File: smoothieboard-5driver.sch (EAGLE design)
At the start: 304 parts, among them IC1 LPC1769, IC10 LM1117-3.3V, IC11 78L12F, IC12 A4982, IC13 R-78E-5.0, IC14 TC4427, IC15 TC4427, IC2 A4982, IC3 A4982, IC4 MCP44X1, IC5 A4982, IC6 A4982, IC9 MCP44X1, J10 POWER_JACKSMD, Q1 BSL207SP, Q10 SUD50P04-08-GE3, Q2 12MHz, Q3 25MHz, Q4 ZXMN4A06, Q5 AOT240L, Q6 AOT240L, Q7 AOT240L, Q8 ZXMN4A06, Q9 ZXMN4A06, U1 USD-SOCKETNEW, X14 USBPTH

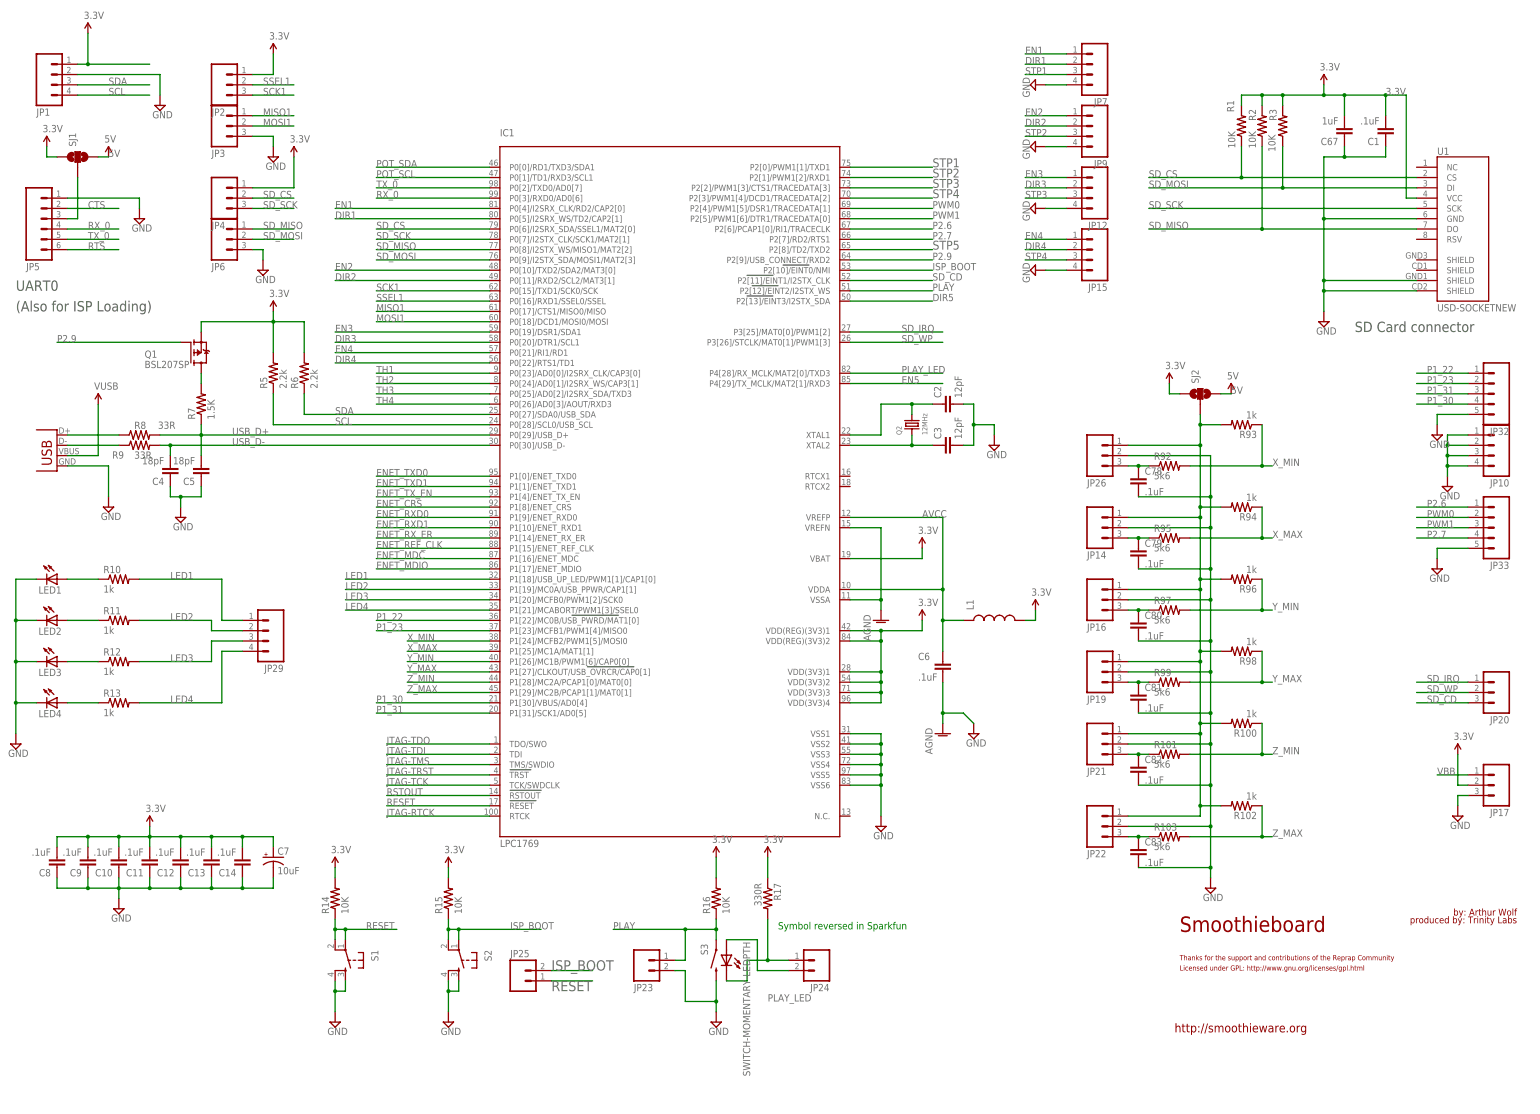
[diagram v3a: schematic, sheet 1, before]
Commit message: Updated R-78 footprint, i2c V select, orientation marker to ic15, silk updates
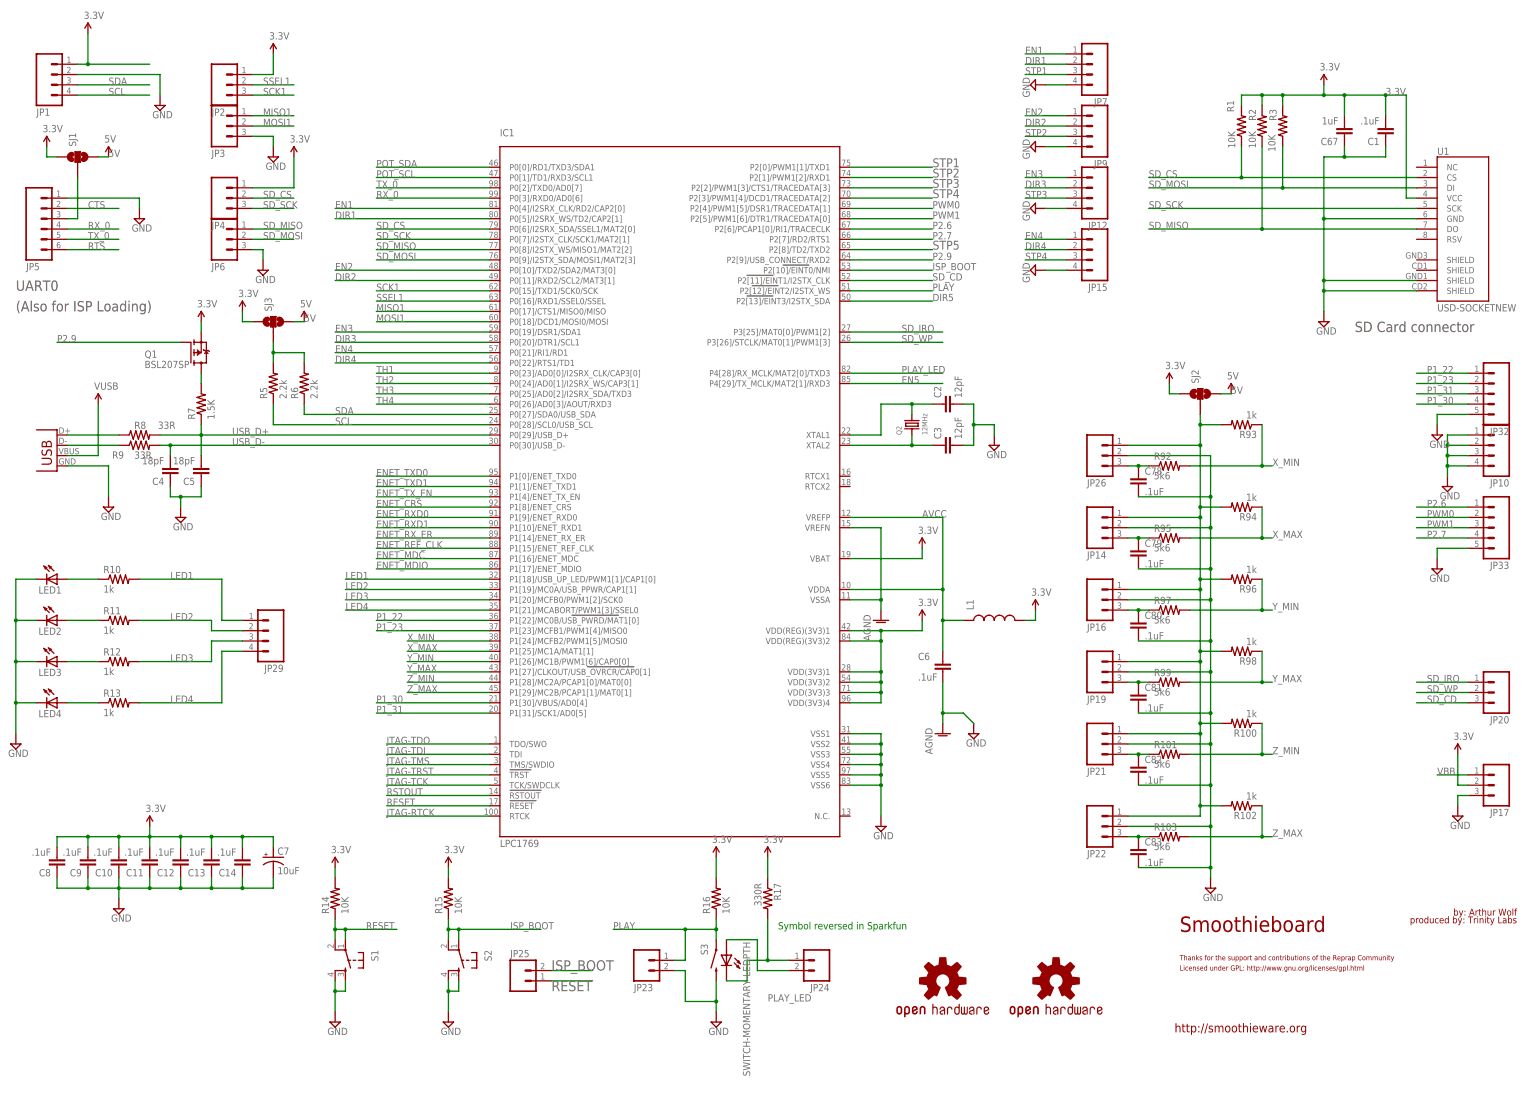
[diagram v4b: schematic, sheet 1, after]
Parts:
- added SJ3: (no value), SparkFun:SOLDERJUMPER_2WAYS
- added U$8, U$9: OSHW-LOGOL, SparkFun-Aesthetics:OSHW-LOGOL
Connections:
- new net N$124: R5.2, R6.2, SJ3.2
- net 3.3V: now also SJ3.1; no longer R5.2, R6.2
- net 5V: now also SJ3.3
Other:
- moved on the sheet: R5, R6
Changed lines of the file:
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@@
 <?xml version="1.0" encoding="utf-8"?>
 <!DOCTYPE eagle SYSTEM "eagle.dtd">
-<eagle version="6.2">
+<eagle version="6.3">
 <drawing>
 <settings>
@@
 <part name="R102" library="resistor" deviceset="R-US_" device="R0603" value="1k"/>
 <part name="R103" library="resistor" deviceset="R-US_" device="R0603" value="5k6"/>
+<part name="SJ3" library="SparkFun" deviceset="SOLDERJUMPER_2WAY" device="S"/>
+<part name="P+40" library="SparkFun" deviceset="3.3V" device=""/>
+<part name="U$2" library="SparkFun" deviceset="5V" device=""/>
+<part name="U$8" library="SparkFun-Aesthetics" deviceset="OSHW-LOGO" device="L"/>
+<part name="U$9" library="SparkFun-Aesthetics" deviceset="OSHW-LOGO" device="L"/>
 </parts>
 <sheets>
@@
 <instance part="SUPPLY58" gate="GND" x="119.38" y="7.62"/>
 <instance part="SUPPLY61" gate="GND" x="43.18" y="205.74"/>
-<instance part="P+30" gate="G$1" x="76.2" y="182.88"/>
-<instance part="R5" gate="G$1" x="76.2" y="167.64" rot="R90"/>
-<instance part="R6" gate="G$1" x="83.82" y="167.64" rot="R90"/>
+<instance part="P+30" gate="G$1" x="58.42" y="180.34"/>
+<instance part="R5" gate="G$1" x="76.2" y="165.1" rot="R90"/>
+<instance part="R6" gate="G$1" x="83.82" y="165.1" rot="R90"/>
 <instance part="SUPPLY64" gate="GND" x="48.26" y="233.68"/>
 <instance part="S1" gate="S" x="93.98" y="22.86" rot="R270"/>
@@
 <instance part="R102" gate="G$1" x="314.96" y="60.96" rot="R180"/>
 <instance part="R103" gate="G$1" x="297.18" y="53.34"/>
+<instance part="SJ3" gate="G$1" x="76.2" y="180.34" rot="R90"/>
+<instance part="P+40" gate="G$1" x="68.58" y="182.88"/>
+<instance part="U$2" gate="G$1" x="83.82" y="180.34"/>
+<instance part="U$8" gate="G$1" x="241.3" y="17.78"/>
+<instance part="U$9" gate="G$1" x="269.24" y="17.78"/>
 </instances>
 <busses>
@@
 </segment>
 <segment>
-<wire x1="76.2" y1="172.72" x2="76.2" y2="180.34" width="0.1524" layer="91"/>
-<wire x1="76.2" y1="180.34" x2="76.2" y2="182.88" width="0.1524" layer="91"/>
-<wire x1="83.82" y1="172.72" x2="83.82" y2="180.34" width="0.1524" layer="91"/>
-<wire x1="83.82" y1="180.34" x2="76.2" y2="180.34" width="0.1524" layer="91"/>
-<junction x="76.2" y="180.34"/>
-<pinref part="R5" gate="G$1" pin="2"/>
 <pinref part="P+30" gate="G$1" pin="3.3V"/>
-<pinref part="R6" gate="G$1" pin="2"/>
 <wire x1="58.42" y1="177.8" x2="58.42" y2="180.34" width="0.1524" layer="91"/>
-<wire x1="58.42" y1="180.34" x2="76.2" y2="180.34" width="0.1524" layer="91"/>
 <pinref part="Q1" gate="G$1" pin="S"/>
 </segment>
@@
 <wire x1="297.18" y1="162.56" x2="299.72" y2="162.56" width="0.1524" layer="91"/>
 </segment>
+<segment>
+<pinref part="P+40" gate="G$1" pin="3.3V"/>
+<wire x1="68.58" y1="180.34" x2="68.58" y2="182.88" width="0.1524" layer="91"/>
+<pinref part="SJ3" gate="G$1" pin="1"/>
+<wire x1="68.58" y1="180.34" x2="71.12" y2="180.34" width="0.1524" layer="91"/>
+</segment>
 </net>
 <net name="AVCC" class="0">
@@
 <segment>
 <wire x1="129.54" y1="154.94" x2="76.2" y2="154.94" width="0.1524" layer="91"/>
-<wire x1="76.2" y1="154.94" x2="76.2" y2="162.56" width="0.1524" layer="91"/>
+<wire x1="76.2" y1="154.94" x2="76.2" y2="160.02" width="0.1524" layer="91"/>
 <label x="91.44" y="154.94" size="1.778" layer="95"/>
 <pinref part="IC1" gate="G$1" pin="P0[28]/SCL0/USB_SCL"/>
@@
 <net name="SDA" class="0">
 <segment>
-<wire x1="83.82" y1="162.56" x2="83.82" y2="157.48" width="0.1524" layer="91"/>
+<wire x1="83.82" y1="160.02" x2="83.82" y2="157.48" width="0.1524" layer="91"/>
 <wire x1="83.82" y1="157.48" x2="129.54" y2="157.48" width="0.1524" layer="91"/>
 <label x="91.44" y="157.48" size="1.778" layer="95"/>
@@
 <label x="312.42" y="162.56" size="1.778" layer="95"/>
 </segment>
+<segment>
+<pinref part="U$2" gate="G$1" pin="5V"/>
+<pinref part="SJ3" gate="G$1" pin="3"/>
+<wire x1="81.28" y1="180.34" x2="83.82" y2="180.34" width="0.1524" layer="91"/>
+<label x="83.82" y="180.34" size="1.778" layer="95"/>
+</segment>
 </net>
 <net name="N$51" class="0">
@@
 </segment>
 </net>
+<net name="N$124" class="0">
+<segment>
+<wire x1="83.82" y1="170.18" x2="83.82" y2="172.72" width="0.1524" layer="91"/>
+<wire x1="83.82" y1="172.72" x2="76.2" y2="172.72" width="0.1524" layer="91"/>
+<pinref part="R6" gate="G$1" pin="2"/>
+<pinref part="R5" gate="G$1" pin="2"/>
+<wire x1="76.2" y1="170.18" x2="76.2" y2="172.72" width="0.1524" layer="91"/>
+<pinref part="SJ3" gate="G$1" pin="2"/>
+<wire x1="76.2" y1="175.26" x2="76.2" y2="172.72" width="0.1524" layer="91"/>
+<junction x="76.2" y="172.72"/>
+</segment>
+</net>
 </nets>
 </sheet>
@@
 <pinref part="IC2" gate="G$1" pin="MS2"/>
 <pinref part="JP30" gate="A" pin="1"/>
+<label x="58.42" y="246.38" size="1.778" layer="95"/>
 </segment>
 <segment>
@@
 <pinref part="IC2" gate="G$1" pin="MS1"/>
 <pinref part="JP31" gate="A" pin="2"/>
+<label x="63.5" y="241.3" size="1.778" layer="95"/>
 </segment>
 <segment>
@@
 </sheet>
 </sheets>
+<errors>
+</errors>
 </schematic>
 </drawing>

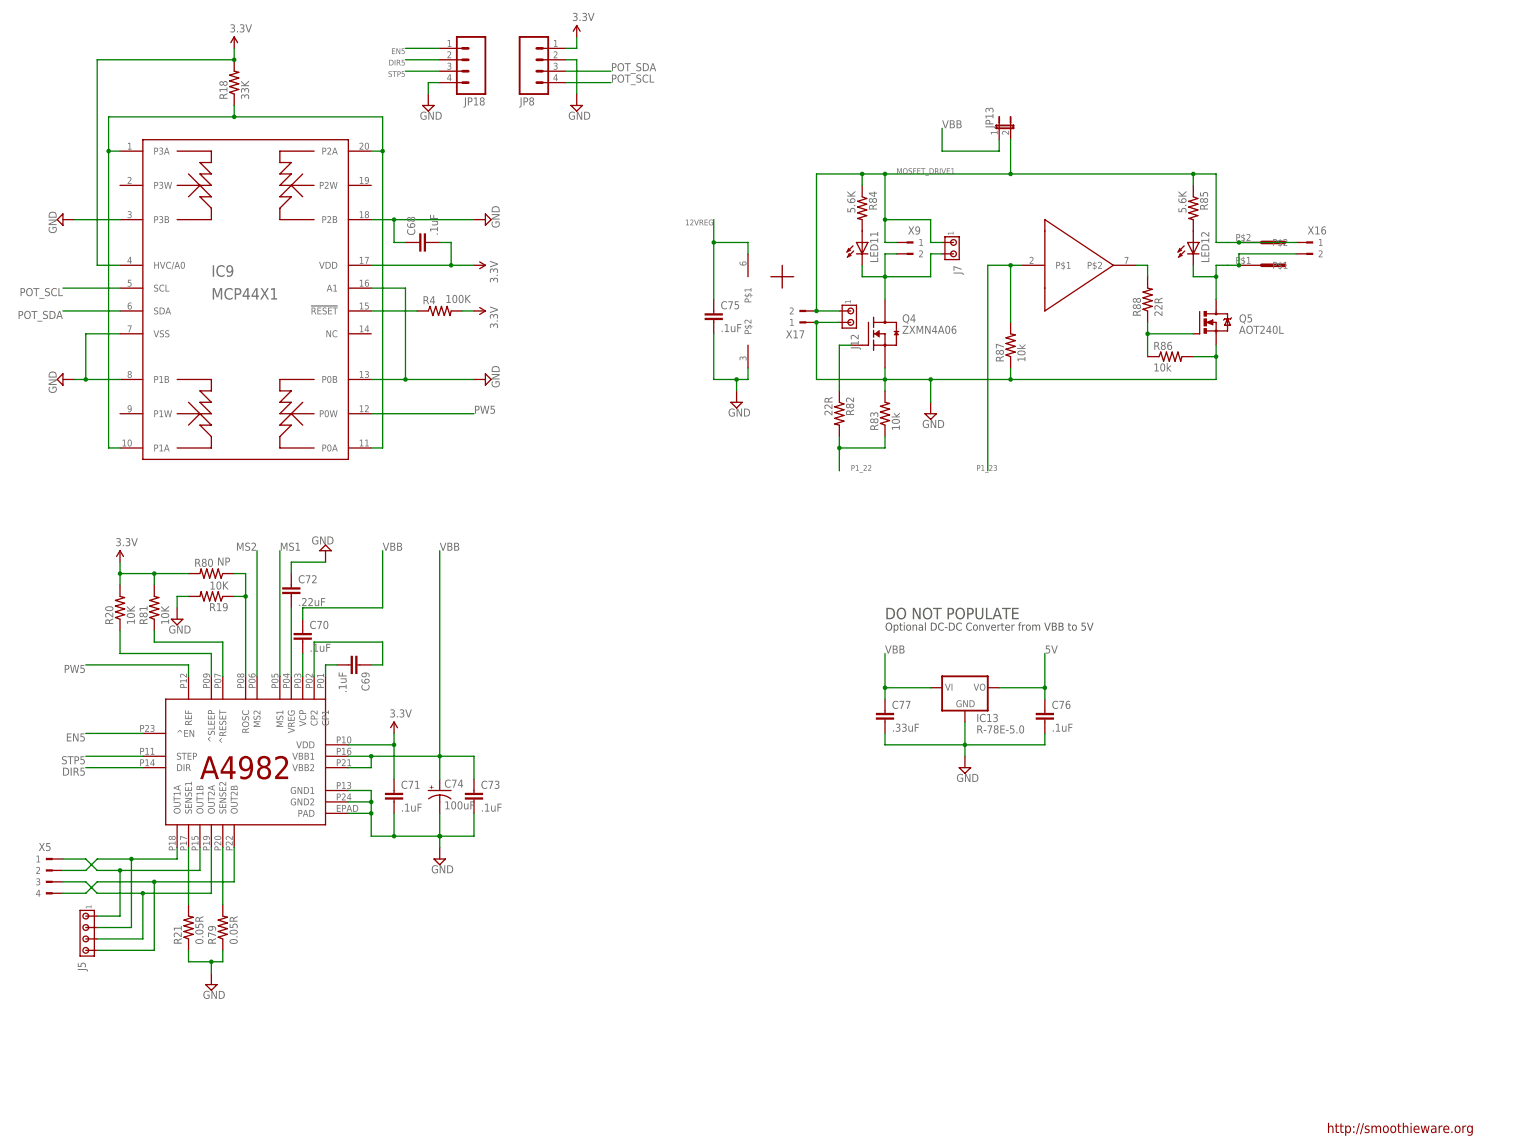
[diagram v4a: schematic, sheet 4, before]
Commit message: Cleaned up connector placement
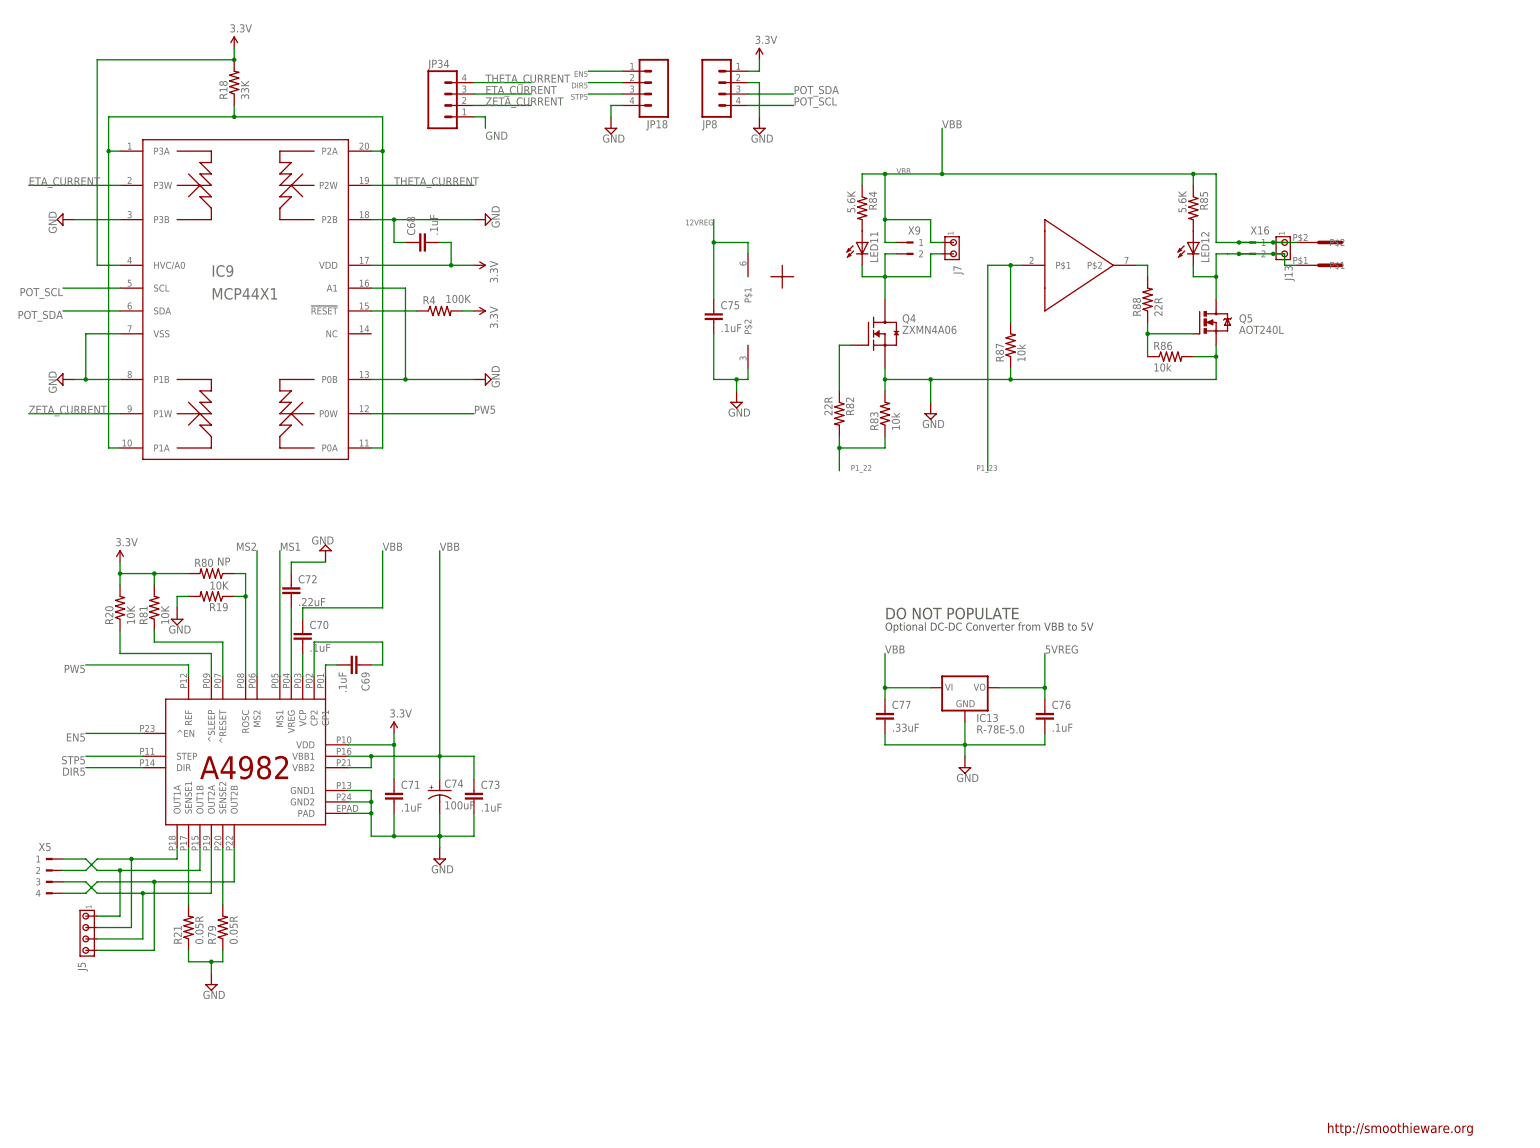
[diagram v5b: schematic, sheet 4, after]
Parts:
- removed J12: (no value), con-amp:MTA02-100
- removed JP13: (no value), jumper:JP1E
- removed X17: (no value), con-weidmueller-sl35:180G-2
- added D6: MBRA210LT3, microbuilder:DIODESMA
- added J11, J13: (no value), con-amp:MTA02-100
- added JP34: (no value), SparkFun:M041X04_NO_SILK
- added U$10: 5MMCONN, eric_sorensen:5MMCONN
- U$8, U$9: value OSHW-LOGOL -> OSHW-LOGOH; device SparkFun-Aesthetics:OSHW-LOGOL -> logxen:OSHW-LOGOH
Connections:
- removed net MOSFET_DRIVE1: J12.1, J7.1, JP13.2, R84.1, R85.1, U$7.P$2, X16.1, X17.2, X9.1
- new net 5VREG: C76.1, D6.A, IC13.VO
- new net ETA_CURRENT: IC9.P3W, JP34.3
- new net THETA_CURRENT: IC9.P2W, JP34.4
- new net ZETA_CURRENT: IC9.P1W, JP34.2
- net 5V: now also D6.C; no longer C76.1, IC13.VO
- net GND: now also JP34.1; no longer J12.2, X17.1
- net MOSFET_DRIVE: now also J11.2, U$10.P$2
- net N$109: now also J13.2
- net N$92: now also U$10.P$1
- net N$94: now also J11.1
- net VBB: now also J13.1, J7.1, R84.1, R85.1, U$7.P$2, X16.1, X9.1; no longer JP13.1
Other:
- moved on the sheet: J9, JP11, JP18, JP28, JP8, X15, X16
